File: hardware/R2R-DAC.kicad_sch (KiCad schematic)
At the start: 28 parts, among them U4 74LVC245A

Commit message: version 1.0
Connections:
- net +3V3: no longer U4.19 (OE)
- net GND: now also U4.19 (OE)
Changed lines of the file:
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@@
   (junction (at 88.9 45.72) (diameter 0) (color 0 0 0 0)
   )
-  (junction (at 54.61 43.18) (diameter 0) (color 0 0 0 0)
+  (junction (at 88.9 50.8) (diameter 0) (color 0 0 0 0)
   )
-  (junction (at 88.9 50.8) (diameter 0) (color 0 0 0 0)
+  (junction (at 69.85 35.56) (diameter 0) (color 0 0 0 0)
   )
   (junction (at 88.9 71.12) (diameter 0) (color 0 0 0 0)
@@
     (stroke (width 0) (type default))
   )
-  (wire (pts (xy 66.04 48.26) (xy 66.04 43.18))
-    (stroke (width 0) (type default))
-  )
   (wire (pts (xy 68.58 53.34) (xy 68.58 45.72))
     (stroke (width 0) (type default))
@@
     (stroke (width 0) (type default))
   )
+  (wire (pts (xy 63.5 40.64) (xy 63.5 35.56))
+    (stroke (width 0) (type default))
+  )
   (wire (pts (xy 66.04 58.42) (xy 71.12 58.42))
     (stroke (width 0) (type default))
@@
   )
   (wire (pts (xy 88.9 76.2) (xy 88.9 80.01))
+    (stroke (width 0) (type default))
+  )
+  (wire (pts (xy 66.04 48.26) (xy 66.04 40.64))
     (stroke (width 0) (type default))
   )
@@
     (stroke (width 0) (type default))
   )
-  (wire (pts (xy 66.04 43.18) (xy 54.61 43.18))
-    (stroke (width 0) (type default))
-  )
   (wire (pts (xy 85.09 66.04) (xy 88.9 66.04))
     (stroke (width 0) (type default))
@@
   )
   (wire (pts (xy 69.85 35.56) (xy 74.93 35.56))
+    (stroke (width 0) (type default))
+  )
+  (wire (pts (xy 63.5 35.56) (xy 69.85 35.56))
     (stroke (width 0) (type default))
   )
@@
     (stroke (width 0) (type default))
   )
+  (wire (pts (xy 66.04 40.64) (xy 63.5 40.64))
+    (stroke (width 0) (type default))
+  )

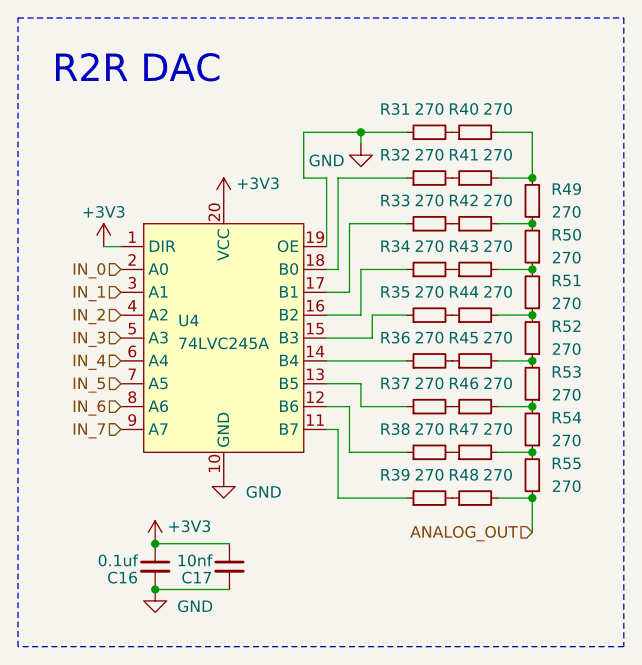
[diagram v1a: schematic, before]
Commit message: fixed error in sync buffer OE pin
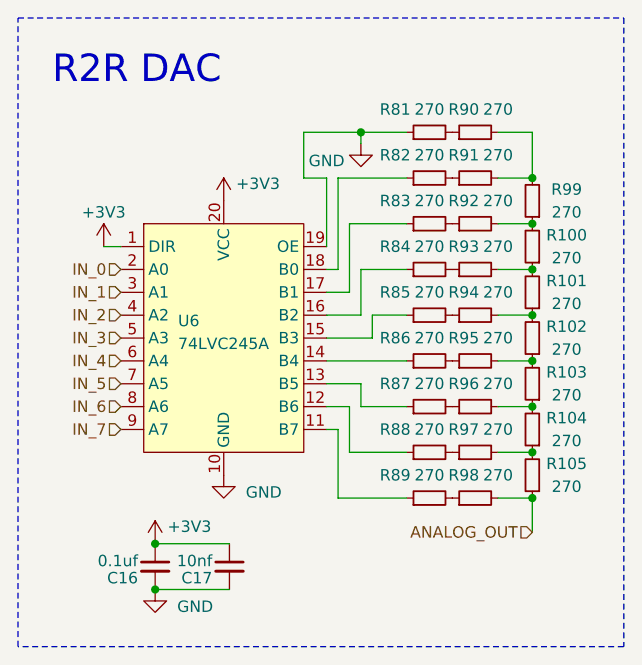
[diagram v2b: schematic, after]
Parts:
- renumbered R50 to R100, R51 to R101, R52 to R102, R53 to R103, R54 to R104, R55 to R105, R31 to R81, R32 to R82, R33 to R83, R34 to R84, R35 to R85, R36 to R86, R37 to R87, R38 to R88, R39 to R89, R40 to R90, R41 to R91, R42 to R92, R43 to R93, R44 to R94, R45 to R95, R46 to R96, R47 to R97, R48 to R98, R49 to R99, U4 to U6
